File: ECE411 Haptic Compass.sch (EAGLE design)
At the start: 15 parts, among them Q1 PBHV8115TLHR, Q2 PBHV8115TLHR, Q3 PBHV8115TLHR, Q4 PBHV8115TLHR, U1 328P

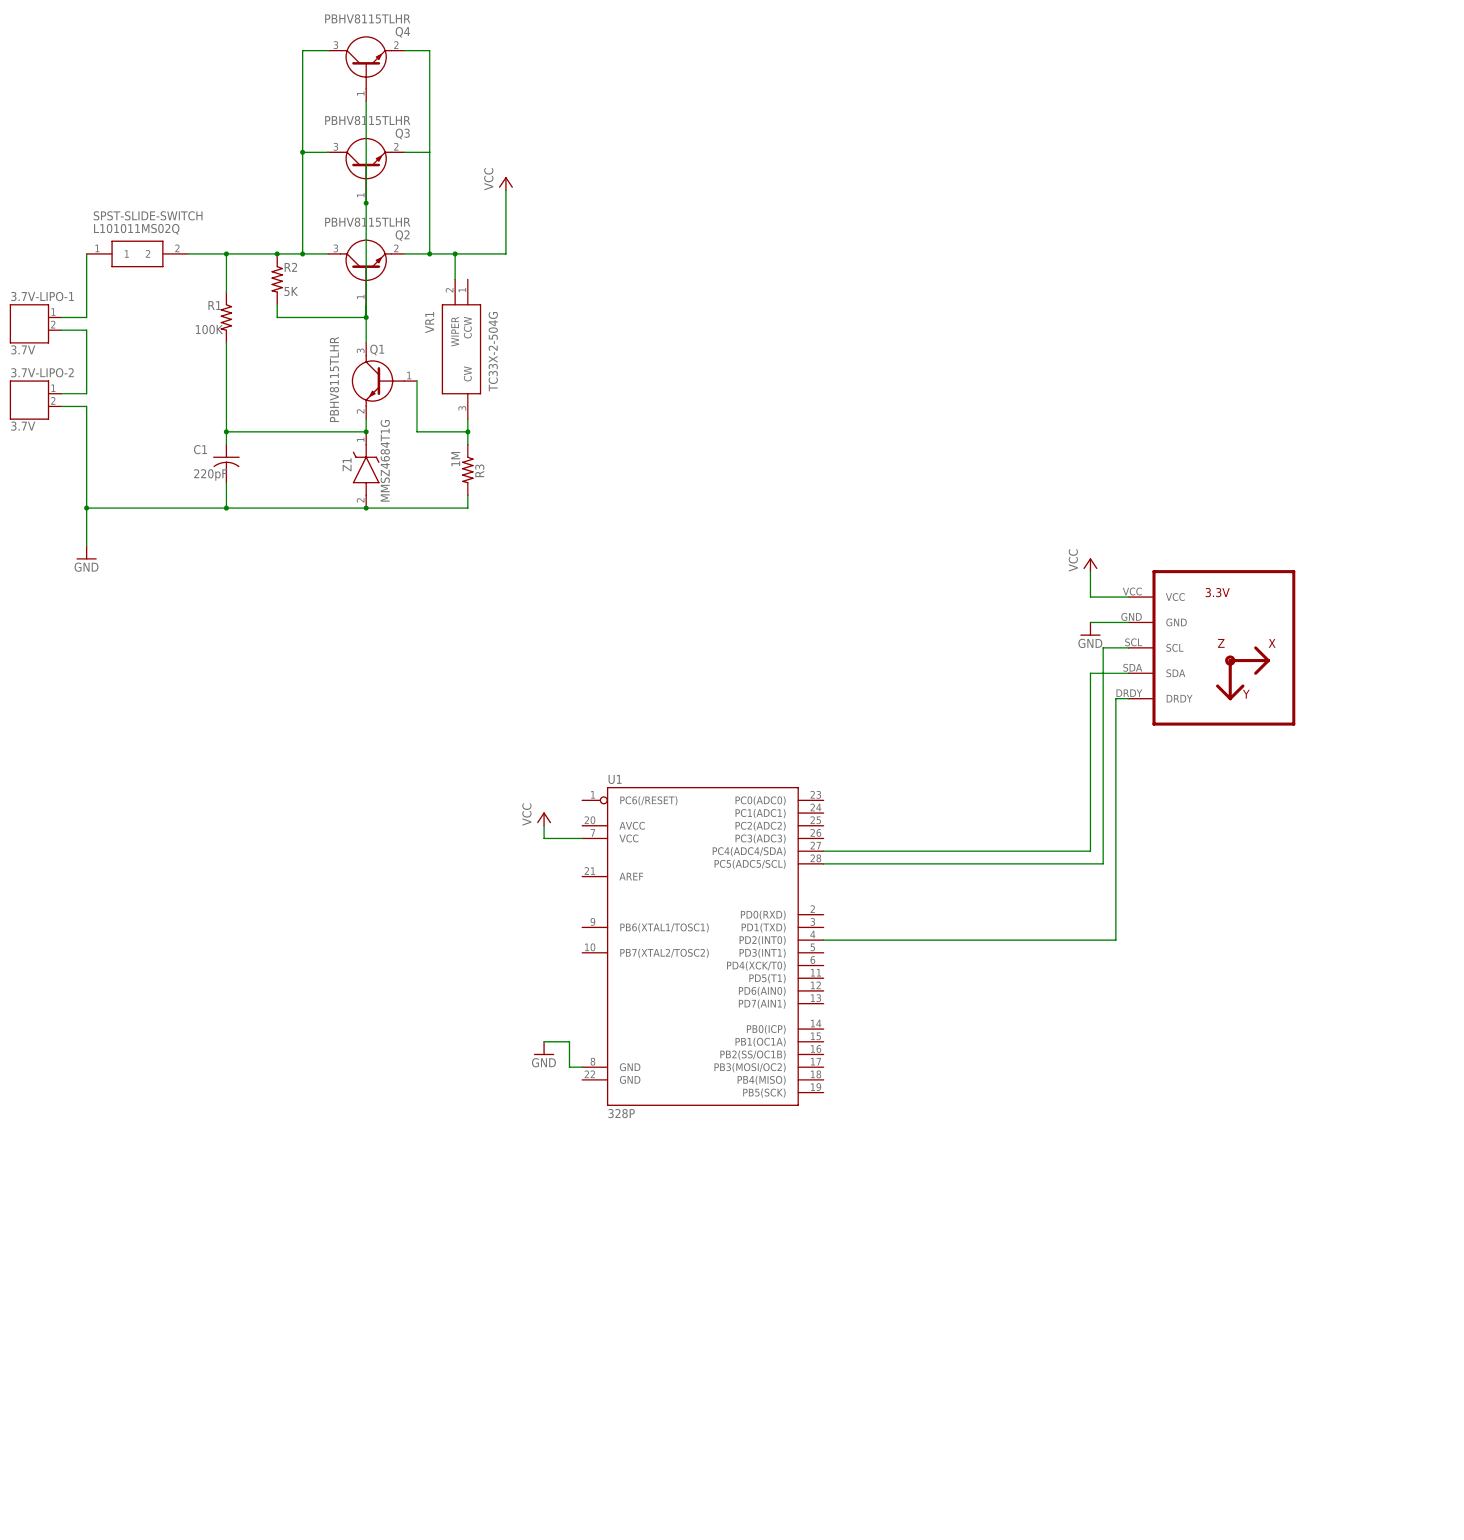
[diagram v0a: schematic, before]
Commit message: Added all modules and I/O
Note that the Magnetic Sensing Module is there as a placeholder. The I/O pins are at the bottom for the actual device in creation.
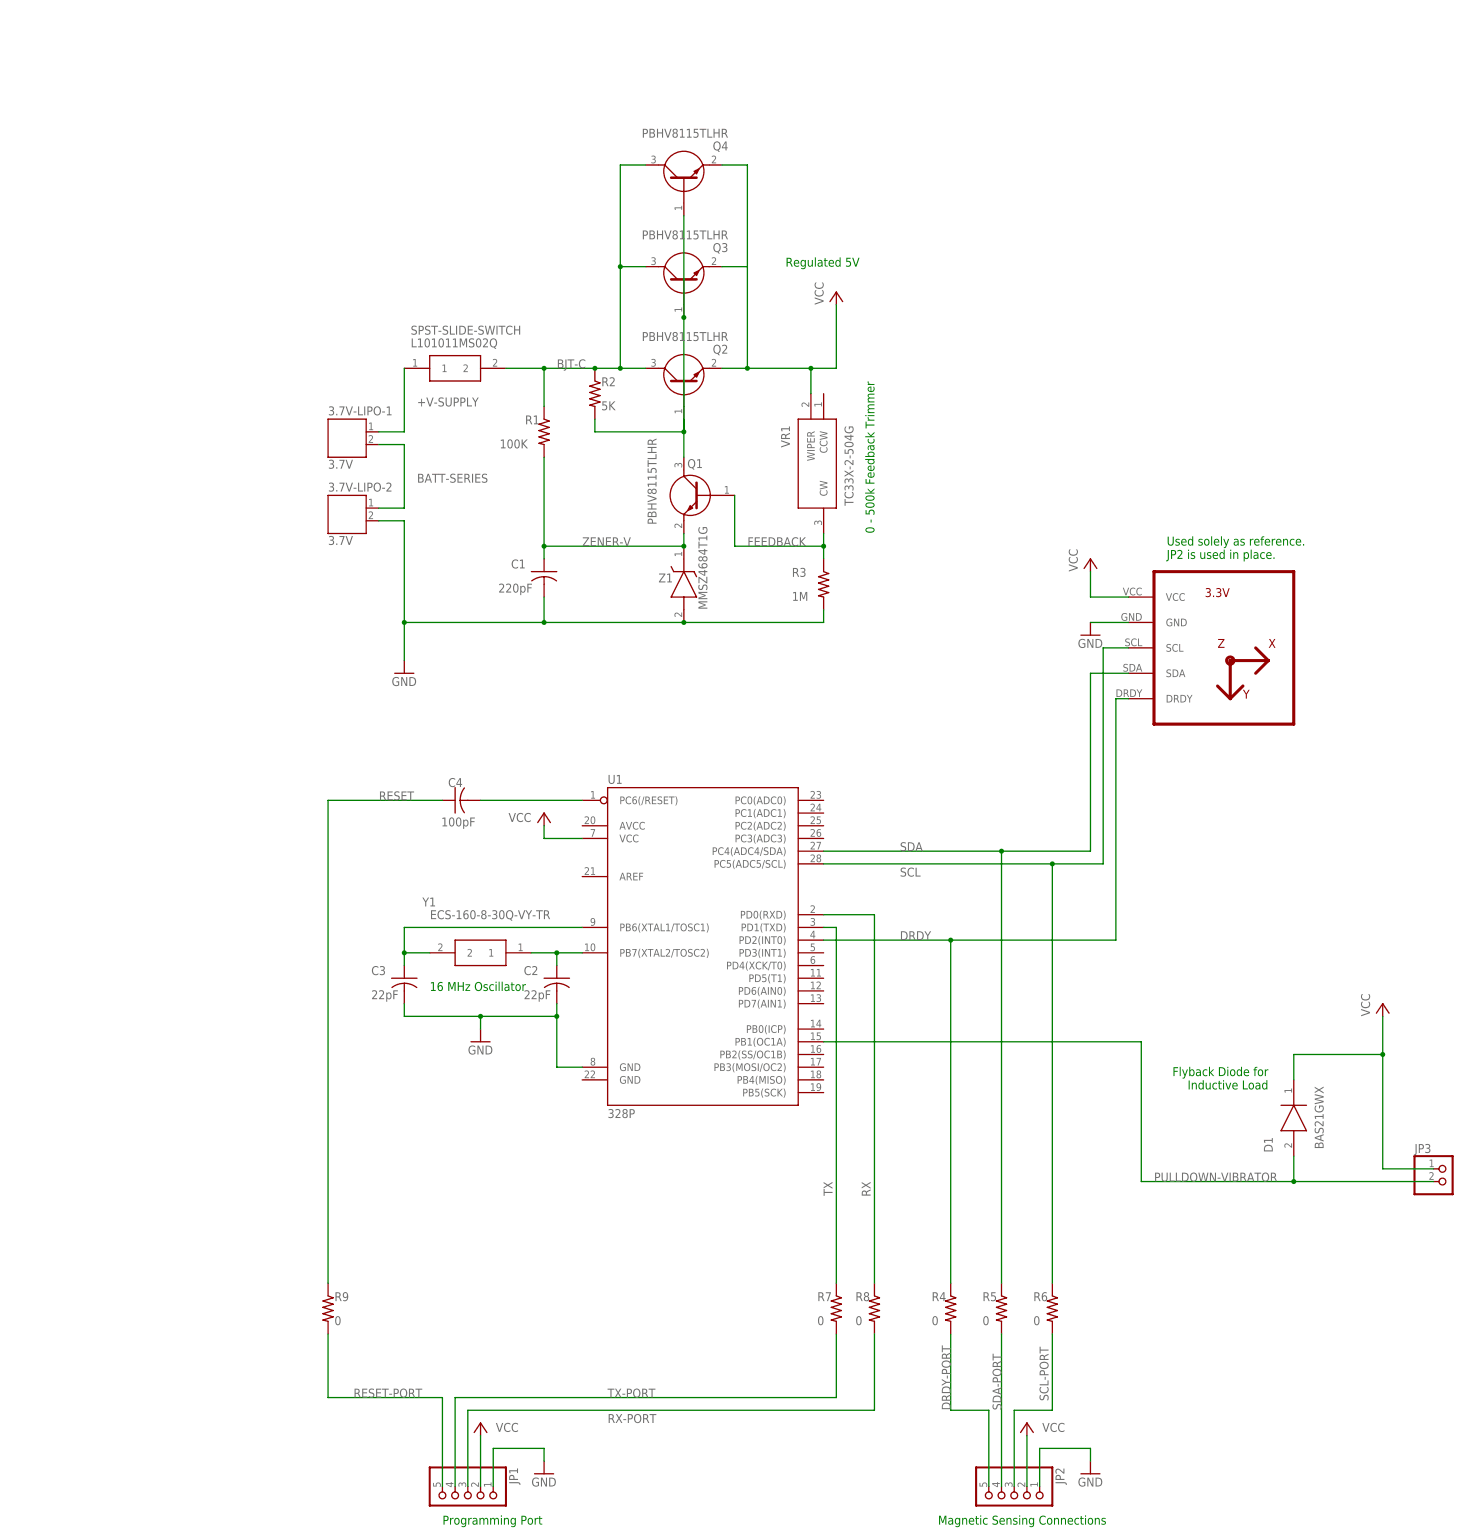
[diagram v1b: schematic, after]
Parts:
- added C2, C3: 22pF, rcl:C-USC0805
- added C4: 100pF, rcl:C-USC0805
- added D1: BAS21GWX, SamacSys_Parts:BAS21GWX
- added JP1, JP2: (no value), pinhead:PINHD-1X5
- added JP3: (no value), pinhead:PINHD-1X2
- added R4, R5, R6, R7, R8, R9: 0, rcl:R-US_R0805
- added Y1: ECS-160-8-30Q-VY-TR, SamacSys_Parts:ECS-160-8-30Q-VY-TR
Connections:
- net N$10 renamed +V-SUPPLY
- net N$11 renamed ZENER-V
- net N$3 renamed FEEDBACK
- net N$6 renamed BATT-SERIES
- net N$8 renamed BJT-C
- removed net N$1: MAGNETOMETER.SDA, U1.PC4(ADC4/SDA)
- removed net N$2: MAGNETOMETER.SCL, U1.PC5(ADC5/SCL)
- removed net N$4: MAGNETOMETER.DRDY, U1.PD2(INT0)
- new net DRDY: MAGNETOMETER.DRDY, R4.1, U1.PD2(INT0)
- new net DRDY-PORT: JP2.5, R4.2
- new net N$15: JP2.2
- new net N$16: C4.2, U1.PC6(/RESET)
- new net N$5: C2.1, U1.PB7(XTAL2/TOSC2), Y1.1
- new net N$7: C3.1, U1.PB6(XTAL1/TOSC1), Y1.2
- new net PULLDOWN-VIBRATOR: D1.A, JP3.2, U1.PB1(OC1A)
- new net RESET: C4.1, R9.1
- new net RESET-PORT: JP1.5, R9.2
- new net RX: R8.1, U1.PD0(RXD)
- new net RX-PORT: JP1.3, R8.2
- new net SCL: MAGNETOMETER.SCL, R6.1, U1.PC5(ADC5/SCL)
- new net SCL-PORT: JP2.3, R6.2
- new net SDA: MAGNETOMETER.SDA, R5.1, U1.PC4(ADC4/SDA)
- new net SDA-PORT: JP2.4, R5.2
- new net TX: R7.1, U1.PD1(TXD)
- new net TX-PORT: JP1.4, R7.2
- net GND: now also C2.2, C3.2, JP1.1, JP2.1
- net VCC: now also D1.K, JP1.2, JP3.1
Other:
- note added: "0 - 500k Feedback Trimmer"
- note added: "16 MHz Oscillator"
- note added: "Flyback Diode for Inductive Load"
- note added: "Magnetic Sensing Connections"
- note added: "Programming Port"
- note added: "Regulated 5V"
- note added: "Used solely as reference. JP2 is used in place."
- moved on the sheet: 3.7V-LIPO-1, 3.7V-LIPO-2, C1, Q1, Q2, Q3, Q4, R1, R2, R3, SPST-SLIDE-SWITCH, VR1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

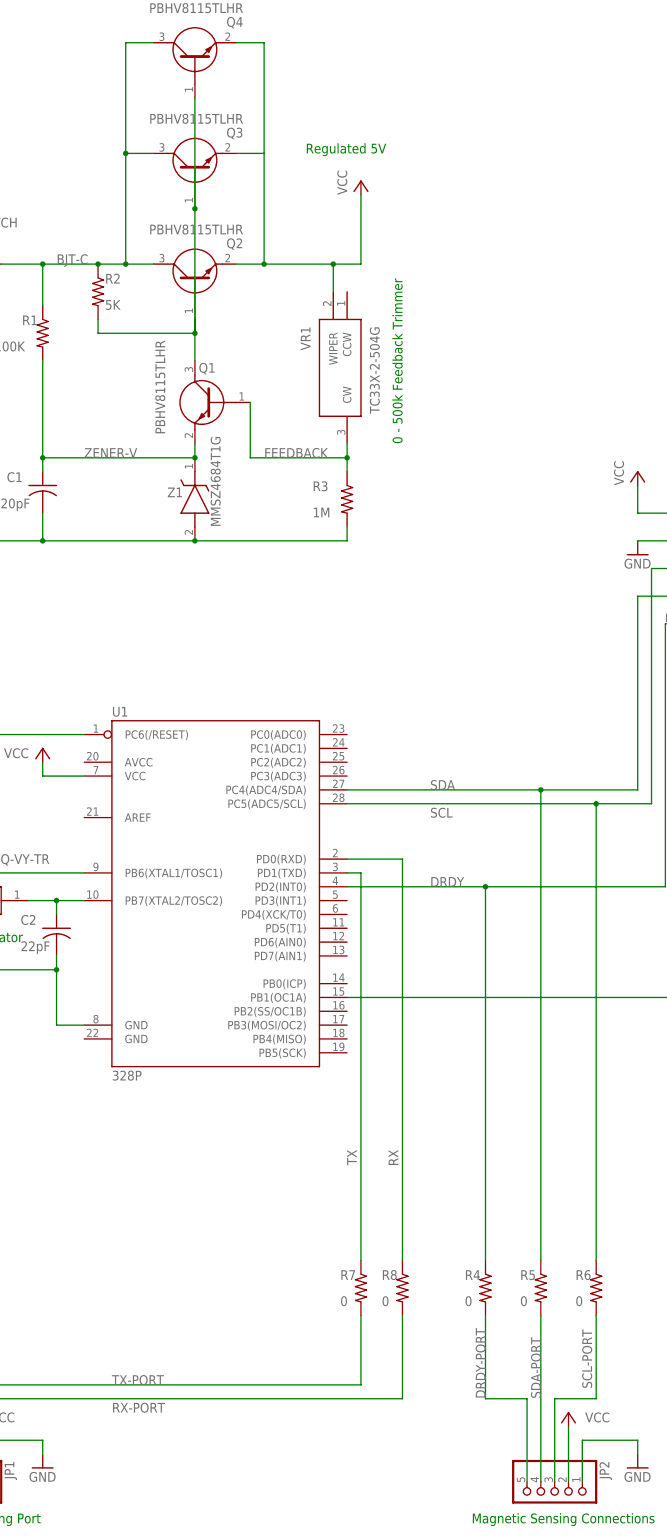
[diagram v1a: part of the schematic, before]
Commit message: Minor Fixes (ERC)
Fixed junction errors and Vcc connection errors.
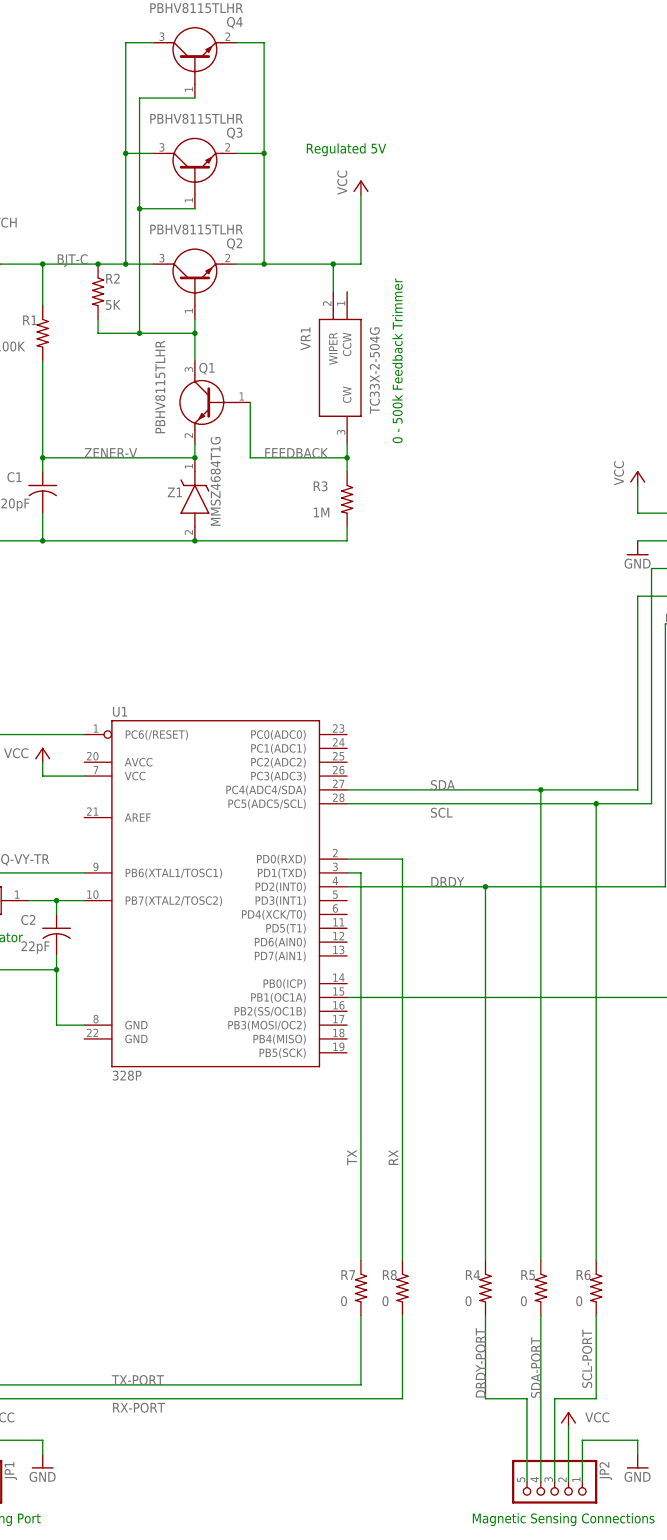
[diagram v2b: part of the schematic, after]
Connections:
- removed net N$15: JP2.2
- net VCC: now also JP2.2
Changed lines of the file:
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@@
 <wire x1="88.9" y1="157.48" x2="88.9" y2="170.18" width="0.1524" layer="91" grouprefs="POWER-5V-REGULATED"/>
 <pinref part="P+1" gate="VCC" pin="VCC"/>
+<junction x="71.12" y="177.8"/>
 </segment>
 <segment>
@@
 <junction x="198.12" y="20.32" grouprefs="VIBRATING-MOTOR"/>
 <pinref part="P+6" gate="VCC" pin="VCC"/>
+</segment>
+<segment>
+<pinref part="P+5" gate="VCC" pin="VCC"/>
+<pinref part="JP2" gate="A" pin="2"/>
+<wire x1="127" y1="-55.88" x2="127" y2="-66.04" width="0.1524" layer="91"/>
 </segment>
 </net>
@@
 <pinref part="R2" gate="G$1" pin="2"/>
 <wire x1="40.64" y1="147.32" x2="40.64" y2="144.78" width="0.1524" layer="91" grouprefs="POWER-5V-REGULATED"/>
-<wire x1="40.64" y1="144.78" x2="58.42" y2="144.78" width="0.1524" layer="91" grouprefs="POWER-5V-REGULATED"/>
+<wire x1="40.64" y1="144.78" x2="48.26" y2="144.78" width="0.1524" layer="91" grouprefs="POWER-5V-REGULATED"/>
 <pinref part="Q2" gate="G$1" pin="B"/>
+<wire x1="48.26" y1="144.78" x2="58.42" y2="144.78" width="0.1524" layer="91" grouprefs="POWER-5V-REGULATED"/>
 <wire x1="58.42" y1="144.78" x2="58.42" y2="147.32" width="0.1524" layer="91" grouprefs="POWER-5V-REGULATED"/>
 <junction x="58.42" y="144.78" grouprefs="POWER-5V-REGULATED"/>
-<pinref part="Q3" gate="G$1" pin="B"/>
-<wire x1="58.42" y1="167.64" x2="58.42" y2="144.78" width="0.1524" layer="91" grouprefs="POWER-5V-REGULATED"/>
-<pinref part="Q4" gate="G$1" pin="B"/>
-<wire x1="58.42" y1="187.96" x2="58.42" y2="167.64" width="0.1524" layer="91" grouprefs="POWER-5V-REGULATED"/>
-<junction x="58.42" y="167.64" grouprefs="POWER-5V-REGULATED"/>
 <pinref part="Q1" gate="G$1" pin="C"/>
 <wire x1="58.42" y1="139.7" x2="58.42" y2="144.78" width="0.1524" layer="91" grouprefs="POWER-5V-REGULATED"/>
+<pinref part="Q4" gate="G$1" pin="B"/>
+<wire x1="48.26" y1="144.78" x2="48.26" y2="167.64" width="0.1524" layer="91"/>
+<wire x1="48.26" y1="167.64" x2="48.26" y2="187.96" width="0.1524" layer="91"/>
+<wire x1="48.26" y1="187.96" x2="58.42" y2="187.96" width="0.1524" layer="91"/>
+<junction x="48.26" y="144.78"/>
+<pinref part="Q3" gate="G$1" pin="B"/>
+<wire x1="48.26" y1="167.64" x2="58.42" y2="167.64" width="0.1524" layer="91"/>
+<junction x="48.26" y="167.64"/>
 </segment>
 </net>
@@
 </segment>
 </net>
-<net name="N$15" class="0">
-<segment>
-<pinref part="JP2" gate="A" pin="2"/>
-<wire x1="127" y1="-66.04" x2="127" y2="-55.88" width="0.1524" layer="91" grouprefs="MAGNETOMETER-IO"/>
-<pinref part="P+5" gate="VCC" pin="VCC"/>
-</segment>
-</net>
